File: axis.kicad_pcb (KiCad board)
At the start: 4 copper layers, 66 x 18 mm, 47 parts, among them J101 CORTEX-DEBUG, J102 JAE_DX07S016JA3, SW101 SW_Push, SW102 SW_Push, U101 BHI160, U102 ATSAMD51G, U103 BMM150, U104 AP2112K-3.3, Y101 32k768

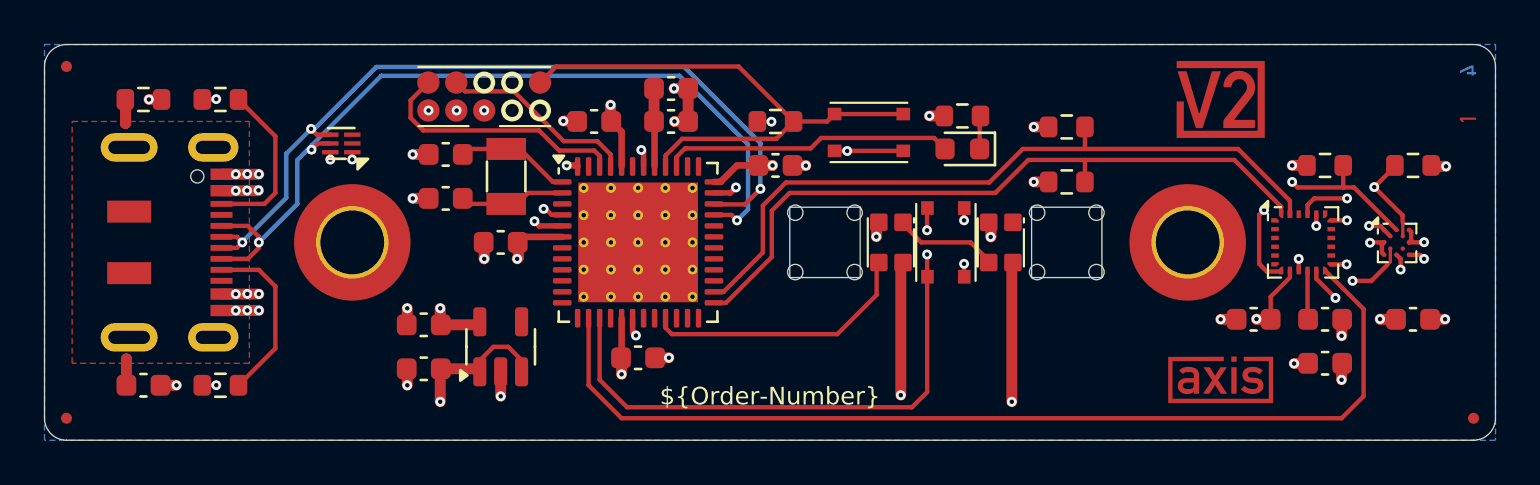
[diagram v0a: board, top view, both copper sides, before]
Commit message: Replace LDO
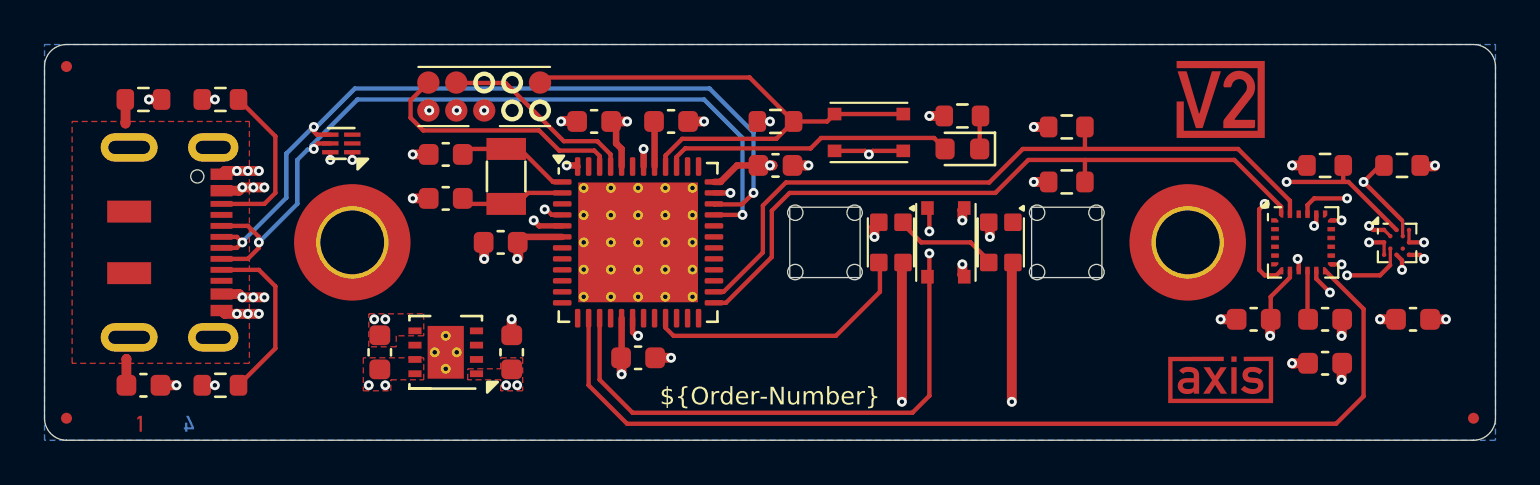
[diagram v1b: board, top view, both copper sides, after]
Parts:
- removed the C104 at (145.5, 100.5)
- removed the C114 at (134.2, 111.8)
- removed the U104 at (137.8, 110.8)
- added C106: 10u, Capacitor_SMD:C_0603_1608Metric, F.Cu at (132.2, 111.0)
- added U101: TPS78433QWDRBRQ1, V2_Package_SON:VSON-8-1_3x3mm_P0.65_EP1.65x2.4mm, F.Cu at (135.2, 111.0)
- moved INFO101 61.1 mm to (122.5, 114.2), turned to 0 degrees
- moved C107 4.19 mm to (138.2, 111.0), turned to 90 degrees
- moved C101 1.50 mm to (145.5, 100.5)
- moved R108 0.50 mm to (178.8, 102.5)
- renumbered C103 to C101, C108 to C102, C109 to C103, C110 to C104, C111 to C105, C112 to C107, C101 to C108, C102 to C109, C116 to C110, C105 to C111, C107 to C112, C106 to C114, D102 to D101, D103 to D102, D101 to D103, ICON102 to ICON101, ICON101 to ICON102, INFO102 to INFO101, INFO101 to INFO102, R106 to R101, R107 to R102, R108 to R103, R109 to R104, R103 to R105, R101 to R106, R102 to R107, R104 to R108, R105 to R109, SW102 to SW101, SW101 to SW102, U101 to U104
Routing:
- net +5V: track 23.0 -> 17.1 mm, vias 10 -> 11
- net GND: track 34.8 -> 30.8 mm, vias 45 -> 44
- net +3V3: track 25.6 -> 22.9 mm, vias 18 -> 19
- net /VDDCORE: track 3.56 -> 2.06 mm
- net /USB-: track 38.1 -> 36.8 mm
- net /USB+: track 37.1 -> 36.0 mm
- net /Button: track 26.9 -> 27.4 mm
- added copper zone on F.Cu, net +3V3
- added copper zone on F.Cu, net +5V
- added copper zone on F.Cu, net GND
- added copper zone on In2.Cu, net GND

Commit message: Update
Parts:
- moved FID102 0.50 mm to (118.0, 98.5)
- moved C101 0.25 mm to (145.5, 100.8)
- moved C102 0.25 mm to (150.2, 102.8)
- moved C103 0.25 mm to (142.0, 100.8)
- moved C104 0.25 mm to (144.0, 111.5)
- moved C105 0.25 mm to (137.8, 106.2)
- moved C106 0.25 mm to (132.2, 111.2)
- moved C107 0.25 mm to (138.2, 111.2)
- moved C108 0.25 mm to (135.2, 102.2)
- moved C109 0.25 mm to (135.2, 104.2)
- moved C110 0.25 mm to (121.5, 112.8)
- moved C111 0.25 mm to (172.0, 109.8)
- moved C112 0.25 mm to (175.2, 111.8)
- moved C113 0.25 mm to (179.2, 109.8)
- moved C114 0.25 mm to (175.2, 109.8)
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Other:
- board size 66 x 18 mm -> 66 x 17.5 mm
